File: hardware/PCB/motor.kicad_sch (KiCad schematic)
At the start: 56 parts, among them J14 Turntable Stepper, J15 Extruder Stepper, J16 Cutting Tool, J17 Gantry Stepper, J18 Revolute Stepper, U10 BSC050N04LSG

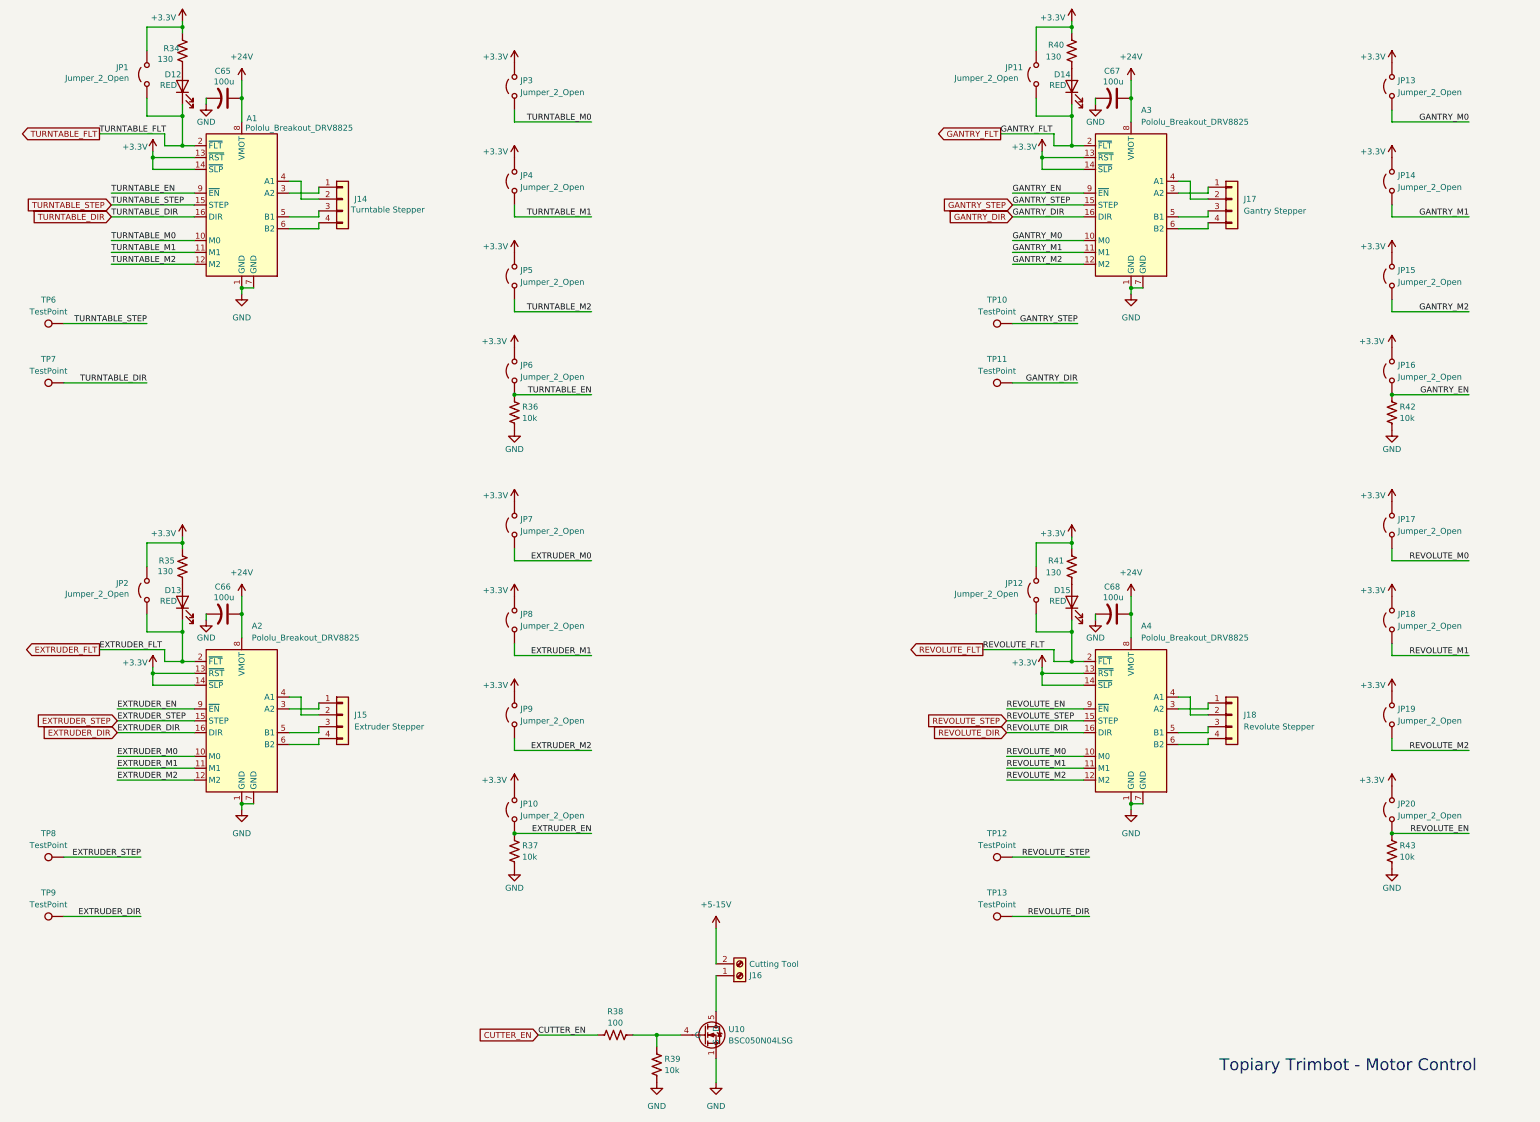
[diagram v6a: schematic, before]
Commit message: Small fixes for stepper drivers plus support for MP6603
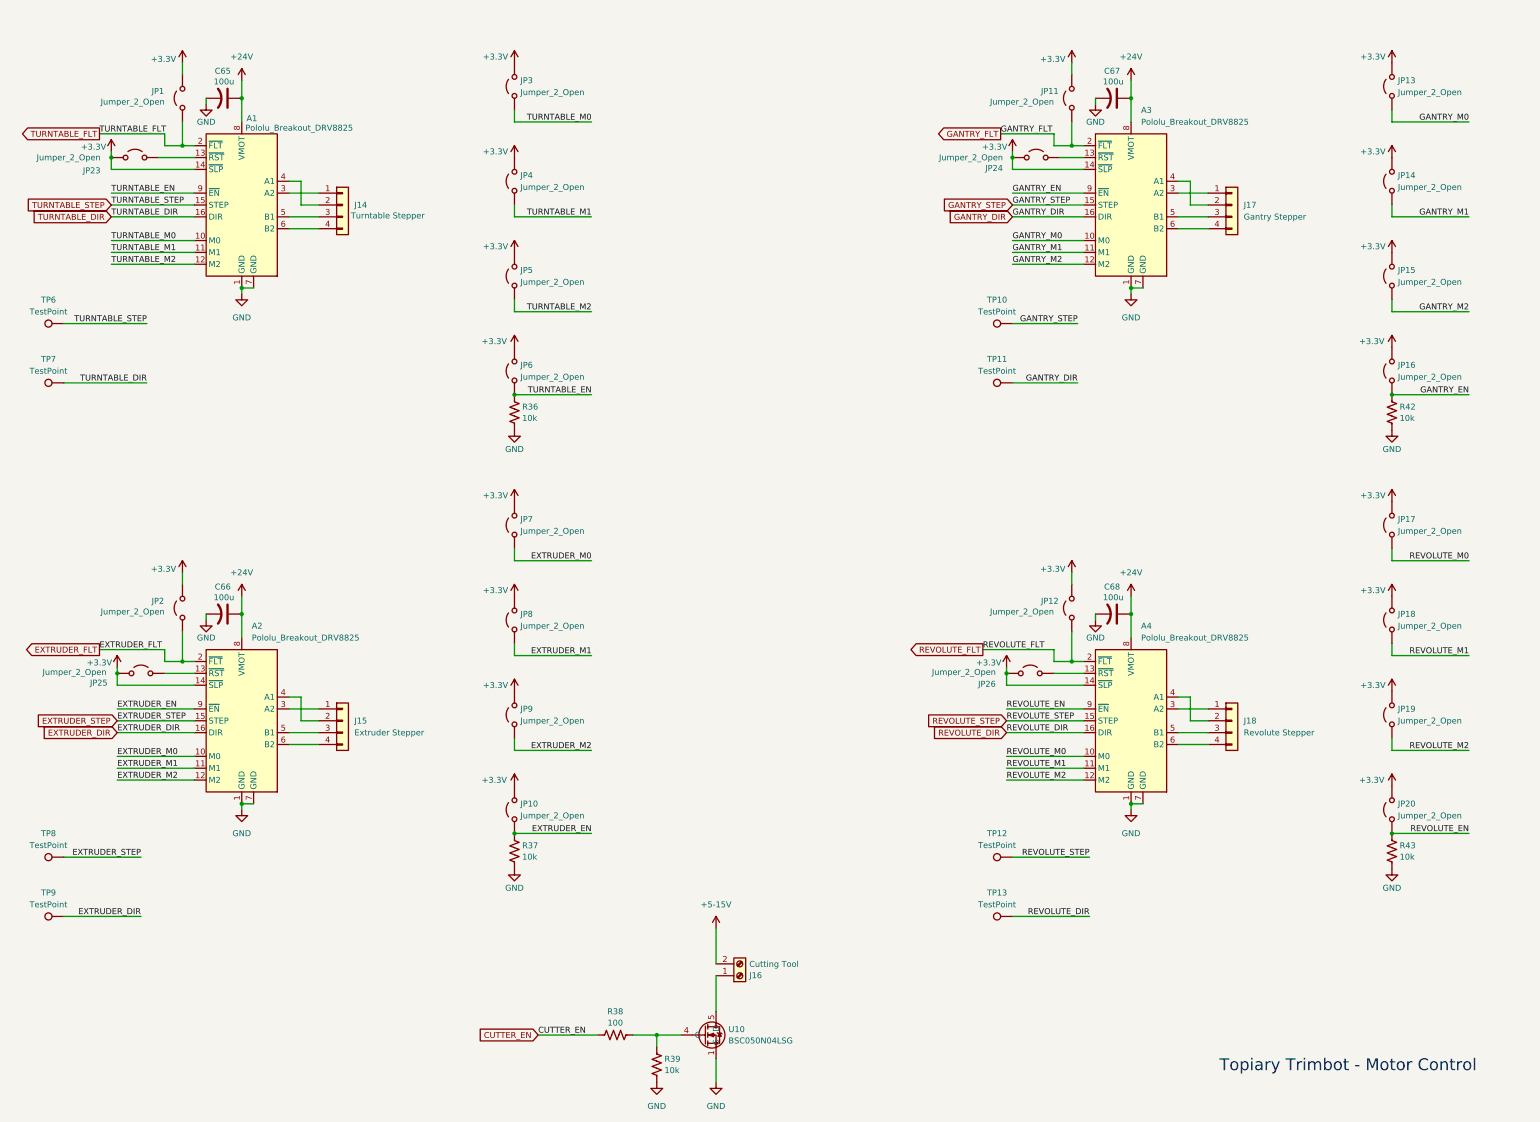
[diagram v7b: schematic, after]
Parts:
- removed D12, D13, D14, D15: RED, LED_SMD:LED_0805_2012Metric, symbol Device:LED
- removed R34, R35, R40, R41: 130, Resistor_SMD:R_0805_2012Metric, symbol Device:R_US
- added JP23, JP24, JP25, JP26: Jumper_2_Open, Connector_PinHeader_2.54mm:PinHeader_1x02_P2.54mm_Vertical, symbol Jumper:Jumper_2_Open
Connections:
- net +3.3V: now also JP23.2 (B), JP24.2 (B), JP25.2 (B), JP26.2 (B); no longer A1.13 (~{RST}), A2.13 (~{RST}), A3.13 (~{RST}), A4.13 (~{RST})
- new net: A4.13 (~{RST}), JP26.1 (A)
- new net: A2.13 (~{RST}), JP25.1 (A)
- new net: A3.13 (~{RST}), JP24.1 (A)
- new net: A1.13 (~{RST}), JP23.1 (A)
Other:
- moved on the sheet: J14, J15, J17, J18, JP1, JP11, JP12, JP2

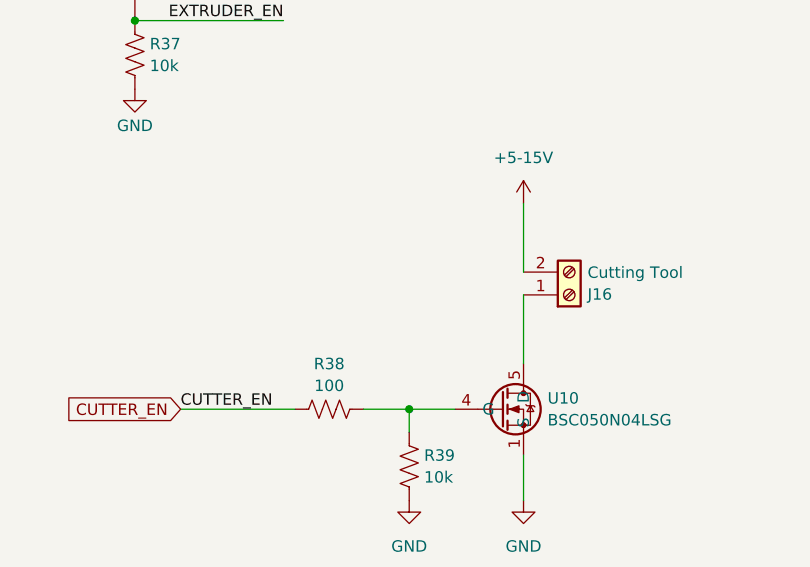
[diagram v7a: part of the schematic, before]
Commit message: Add cutting motor flyback diode and swap flash memory part for MX25L51245
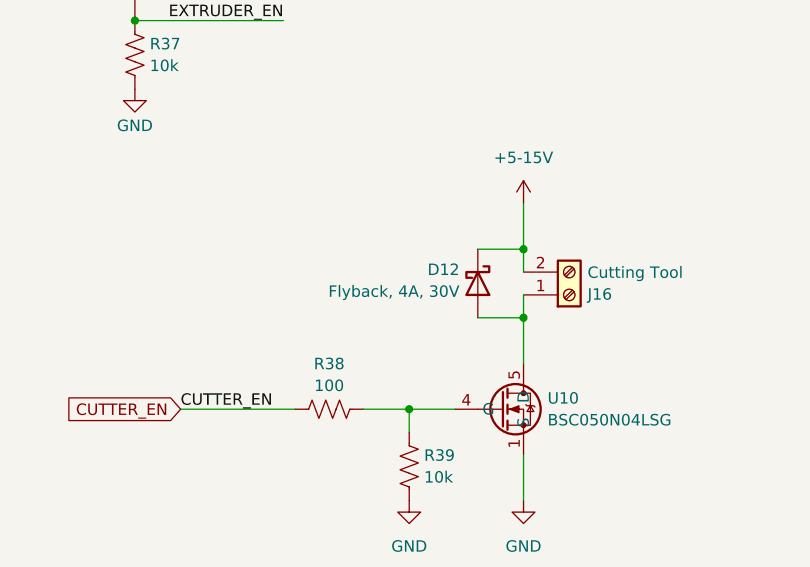
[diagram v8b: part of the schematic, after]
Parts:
- added D12: Flyback, 4A, 30V, Diode_SMD:D_SMA, symbol Device:D_Schottky
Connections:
- net +5-15V: now also D12.1 (K)
- net at J16.1 (Pin_1), U10.5 (D): now also D12.2 (A)
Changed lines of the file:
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@@
 	)
 	(junction
+		(at 203.2 236.22)
+		(diameter 0)
+		(color 0 0 0 0)
+	)
+	(junction
 		(at 160.02 116.84)
 		(diameter 0)
@@
 	)
 	(junction
+		(at 203.2 243.84)
+		(diameter 0)
+		(color 0 0 0 0)
+	)
+	(junction
 		(at 101.6 53.34)
 		(diameter 0)
@@
 	(wire
 		(pts
+			(xy 203.2 243.84) (xy 203.2 248.92)
+		)
+		(stroke
+			(width 0)
+			(type default)
+		)
+	)
+	(wire
+		(pts
 			(xy 73.66 68.58) (xy 73.66 66.04)
 		)
@@
 	(wire
 		(pts
+			(xy 203.2 236.22) (xy 203.2 238.76)
+		)
+		(stroke
+			(width 0)
+			(type default)
+		)
+	)
+	(wire
+		(pts
 			(xy 73.66 73.66) (xy 91.44 73.66)
 		)
@@
 	(wire
 		(pts
-			(xy 203.2 241.3) (xy 203.2 248.92)
+			(xy 203.2 241.3) (xy 203.2 243.84)
 		)
 		(stroke
@@
 	(wire
 		(pts
+			(xy 198.12 236.22) (xy 203.2 236.22)
+		)
+		(stroke
+			(width 0)
+			(type default)
+		)
+	)
+	(wire
+		(pts
 			(xy 160.02 152.4) (xy 160.02 149.86)
 		)
@@
 	(wire
 		(pts
+			(xy 198.12 243.84) (xy 203.2 243.84)
+		)
+		(stroke
+			(width 0)
+			(type default)
+		)
+	)
+	(wire
+		(pts
 			(xy 302.26 184.15) (xy 308.61 184.15)
 		)
@@
 	(wire
 		(pts
-			(xy 203.2 231.14) (xy 203.2 238.76)
+			(xy 203.2 231.14) (xy 203.2 236.22)
 		)
 		(stroke
@@
 					(unit 1)
 				)
+			)
+		)
+	)
+	(symbol
+		(lib_id "Device:D_Schottky")
+		(at 198.12 240.03 270)
+		(unit 1)
+		(exclude_from_sim no)
+		(in_bom yes)
+		(on_board yes)
+		(dnp no)
+		(property "Reference" "D12"
+			(at 196.088 238.5003 90)
+			(effects
+				(font
+					(size 1.27 1.27)
+				)
+				(justify right)
+			)
+		)
+		(property "Value" "Flyback, 4A, 30V"
+			(at 196.088 240.9246 90)
+			(effects
+				(font
+					(size 1.27 1.27)
+				)
+				(justify right)
+			)
+		)
+		(property "Footprint" "Diode_SMD:D_SMA"
+			(at 198.12 240.03 0)
+			(effects
+				(font
+					(size 1.27 1.27)
+				)
+				(hide yes)
+			)
+		)
+		(property "Datasheet" "https://www.diodes.com/assets/Datasheets/SDT5A50SA.pdf"
+			(at 198.12 240.03 0)
+			(effects
+				(font
+					(size 1.27 1.27)
+				)
+				(hide yes)
+			)
+		)
+		(property "Description" "Schottky diode"
+			(at 198.12 240.03 0)
+			(effects
+				(font
+					(size 1.27 1.27)
+				)
+				(hide yes)
+			)
+		)
+		(property "Field5" ""
+			(at 198.12 240.03 90)
+			(effects
+				(font
+					(size 1.27 1.27)
+				)
+				(hide yes)
+			)
+		)
+		(property "Field6" ""
+			(at 198.12 240.03 90)
+			(effects
+				(font
+					(size 1.27 1.27)
+				)
+				(hide yes)
+			)
+		)
+		(property "MANUFACTURER" "Diodes Incorporated"
+			(at 198.12 240.03 90)
+			(effects
+				(font
+					(size 1.27 1.27)
+				)
+				(hide yes)
+			)
+		)
+		(property "Manufacturer_Part_Number" "SDT5A50SA-13"
+			(at 198.12 240.03 90)
+			(effects
+				(font
+					(size 1.27 1.27)
+				)
+				(hide yes)
+			)
+		)
+		(pin "1"
+		)
+		(pin "2"
+		)
+		(instances
+			(project ""
+				(path "/2826ff7c-9767-4078-8ea2-1cd3a432abf3/60c25ff0-1584-491b-871e-d697acc05978"
+					(reference "D12")
+					(unit 1)
+				)
